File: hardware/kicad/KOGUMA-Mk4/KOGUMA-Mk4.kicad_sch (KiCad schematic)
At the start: 0 parts

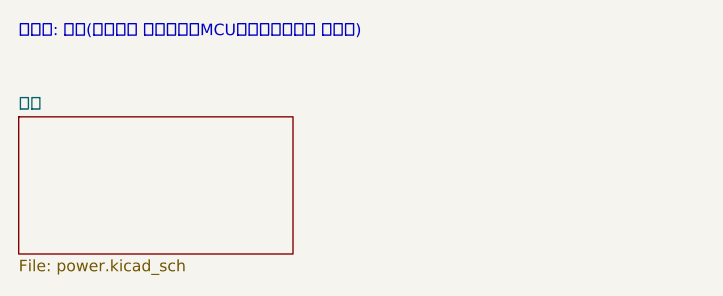
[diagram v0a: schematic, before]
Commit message: モーターのブロックの回路図を作り、MP6551 の電流計測(CM)で進めることを決める
- MP6551 の CM を調べた(精度は typ. のみ、+と−で約25%違う、応答の速さは書かれていない)。
  今の駆動方法(片側の下側のFETをずっと ON)なら電流が常に見えるので、専用ICなしで始め、
  1個ずつ・向きごとに校正する
- RREF を 6.2kΩ × 2 から 4.7kΩ × 2 に(+側が約4.3Aで振り切れるため)、CM に 1nF
- motor.kicad_sch: MP6551 × 2(VIN のパスコン、CM、SR、nFAULT、EN)と吸引ファン
- 記号 MP6551GQB・IRLML6344、フットプリント MPS_QFN-14_2.5x3mm を追加

Co-Authored-By: Claude Opus 5.5 <noreply@anthropic.com>
Claude-Session: https://claude.ai/code/session_01H2Zvpqxqu2v63zaiCMmfT3
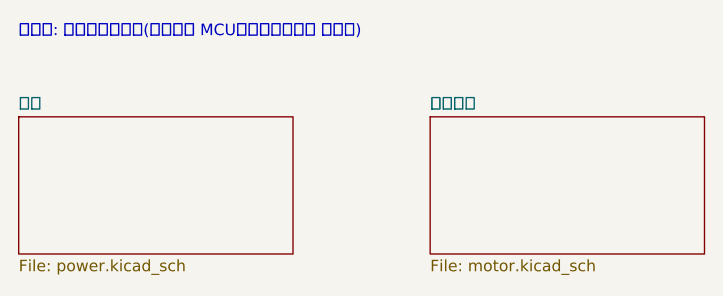
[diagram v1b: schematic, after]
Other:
- added sheet モーター (motor.kicad_sch)
- note added: "シート: 電源・モーター(これから MCU・センサ・表示 を足す)"
- note removed: "シート: 電源(これから モーター・MCU・センサ・表示 を足す)"
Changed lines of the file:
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@@
 		(rev "0.1")
 	)
-	(text "シート: 電源(これから モーター・MCU・センサ・表示 を足す)"
+	(text "シート: 電源・モーター(これから MCU・センサ・表示 を足す)"
 		(exclude_from_sim no)
 		(at 25.4 20.32 0)
@@
 		(instances
 			(project "KOGUMA-Mk4"
-				(path "/9b7d9cce-e694-4ccb-908f-cf46129b4ffc"
+				(path "/b4ecac63-bf9d-5a4c-873b-2154e676a044"
 					(page "2")
 				)
 			)
+		)
+	)
+	(sheet
+		(at 71.12 30.48)
+		(size 30.48 15.24)
+		(exclude_from_sim no)
+		(in_bom yes)
+		(on_board yes)
+		(dnp no)
+		(fields_autoplaced yes)
+		(stroke
+			(width 0.1524)
+			(type solid)
+		)
+		(fill
+			(color 0 0 0 0.0000)
+		)
+		(property "Sheetname" "モーター"
+			(at 71.12 29.7684 0)
+			(effects
+				(font
+					(size 1.27 1.27)
+				)
+				(justify left bottom)
+			)
+		)
+		(property "Sheetfile" "motor.kicad_sch"
+			(at 71.12 46.3046 0)
+			(effects
+				(font
+					(size 1.27 1.27)
+				)
+				(justify left top)
+			)
+		)
+		(instances
+			(project "KOGUMA-Mk4"
+				(path "/b4ecac63-bf9d-5a4c-873b-2154e676a044"
+					(page "3")
+				)
+			)

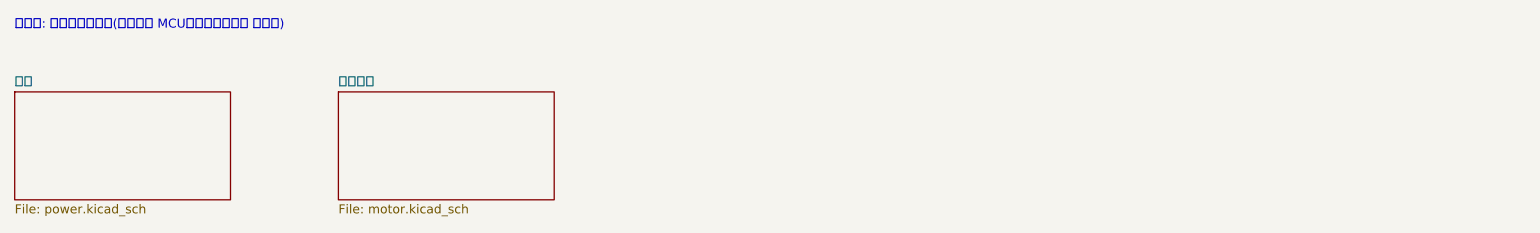
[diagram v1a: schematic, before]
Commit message: MCU のシートを作る(STM32H725RGVx、Direct SMPS、パスコン)
- mcu.kicad_sch: pinmap.md の41本をグローバルラベルで出す(ネットリストで一致を確認)、
  SMPS は DS13311 の図17「Direct SMPS supply」のとおり(L1 2.2µH、VFBSMPS 10µF、VLXSMPS 220pF)、
  VDD ごとの 100nF + 4.7µF、VBAT 100nF、VDDA はフェライトビーズ + 1µF + 100nF、BOOT0 10kΩ、NRST 100nF
- VCAP を 2.2µF × 2 から 100nF × 2 に(表15の注1: LDO を使わないとき。VFQFPN68 は Direct SMPS 専用)
- STM32H725RGVx の記号をプロジェクトに写し、ピンの種類を直す(VLXSMPS を出力、重ねた VCAP を passive)

Co-Authored-By: Claude Opus 5.5 <noreply@anthropic.com>
Claude-Session: https://claude.ai/code/session_01H2Zvpqxqu2v63zaiCMmfT3
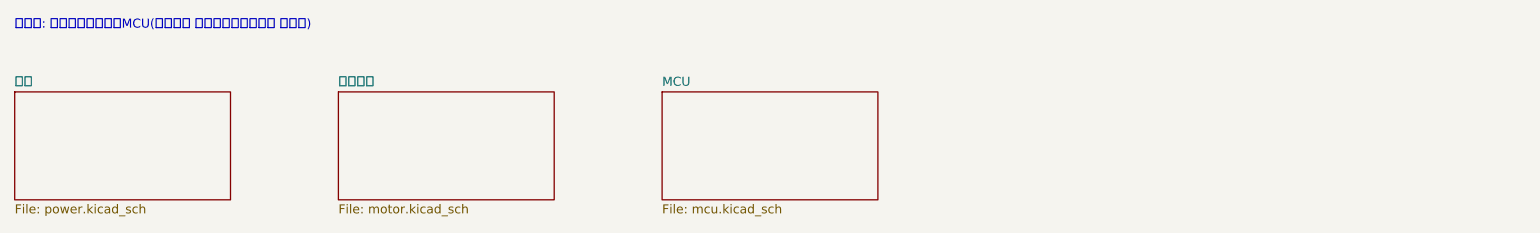
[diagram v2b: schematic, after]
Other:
- added sheet MCU (mcu.kicad_sch)
- note added: "シート: 電源・モーター・MCU(これから センサ・表示・通信 を足す)"
- note removed: "シート: 電源・モーター(これから MCU・センサ・表示 を足す)"
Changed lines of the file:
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@@
 		(rev "0.1")
 	)
-	(text "シート: 電源・モーター(これから MCU・センサ・表示 を足す)"
+	(text "シート: 電源・モーター・MCU(これから センサ・表示・通信 を足す)"
 		(exclude_from_sim no)
 		(at 25.4 20.32 0)
@@
 				)
 			)
+		)
+	)
+	(sheet
+		(at 116.84 30.48)
+		(size 30.48 15.24)
+		(exclude_from_sim no)
+		(in_bom yes)
+		(on_board yes)
+		(dnp no)
+		(fields_autoplaced yes)
+		(stroke
+			(width 0.1524)
+			(type solid)
+		)
+		(fill
+			(color 0 0 0 0.0000)
+		)
+		(property "Sheetname" "MCU"
+			(at 116.84 29.7684 0)
+			(effects
+				(font
+					(size 1.27 1.27)
+				)
+				(justify left bottom)
+			)
+		)
+		(property "Sheetfile" "mcu.kicad_sch"
+			(at 116.84 46.3046 0)
+			(effects
+				(font
+					(size 1.27 1.27)
+				)
+				(justify left top)
+			)
+		)
+		(instances
+			(project "KOGUMA-Mk4"
+				(path "/b4ecac63-bf9d-5a4c-873b-2154e676a044"
+					(page "4")
+				)
+			)

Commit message: センサのシートを作る(壁センサ 4ch、IMU、エンコーダの基板への線)
- sensor.kicad_sch(A3): MK3 の回路(docs/reference)を 3.3V・1個ずつ駆動に合わせて描く。
  発光 OPV332 + NJU6080(20Ω、10mA)× 4、受光 SFH 229 FA + AD8606(820k ∥ 2.2p、PD_BIAS 0.148V)× 4、
  IMU LSM6DSR(SPI3)、エンコーダの基板への6本の線 × 2
- 発光は MK3 と同じく対角の2個ずつ(MK3 のソフトの WallLED_12 / WallLED_34)。
  ネット名を WALL_LED_L / WALL_LED_R から WALL_LED_FL_R / WALL_LED_L_FR に変える
- 記号 NJU6080・LSM6DSR を追加。生成に使う記号の継承(extends)と複数ユニットに対応

Co-Authored-By: Claude Opus 5.5 <noreply@anthropic.com>
Claude-Session: https://claude.ai/code/session_01H2Zvpqxqu2v63zaiCMmfT3
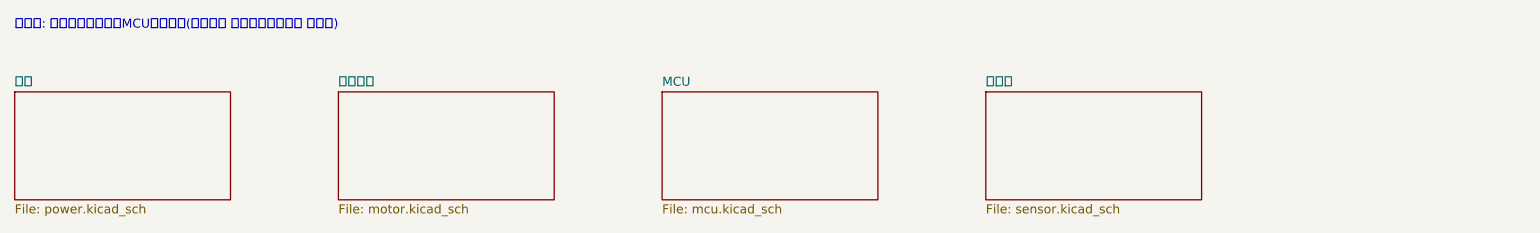
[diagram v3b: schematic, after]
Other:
- added sheet センサ (sensor.kicad_sch)
- note added: "シート: 電源・モーター・MCU・センサ(これから 表示・入力・通信 を足す)"
- note removed: "シート: 電源・モーター・MCU(これから センサ・表示・通信 を足す)"
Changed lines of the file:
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@@
 		(rev "0.1")
 	)
-	(text "シート: 電源・モーター・MCU(これから センサ・表示・通信 を足す)"
+	(text "シート: 電源・モーター・MCU・センサ(これから 表示・入力・通信 を足す)"
 		(exclude_from_sim no)
 		(at 25.4 20.32 0)
@@
 				)
 			)
+		)
+	)
+	(sheet
+		(at 162.56 30.48)
+		(size 30.48 15.24)
+		(exclude_from_sim no)
+		(in_bom yes)
+		(on_board yes)
+		(dnp no)
+		(fields_autoplaced yes)
+		(stroke
+			(width 0.1524)
+			(type solid)
+		)
+		(fill
+			(color 0 0 0 0.0000)
+		)
+		(property "Sheetname" "センサ"
+			(at 162.56 29.7684 0)
+			(effects
+				(font
+					(size 1.27 1.27)
+				)
+				(justify left bottom)
+			)
+		)
+		(property "Sheetfile" "sensor.kicad_sch"
+			(at 162.56 46.3046 0)
+			(effects
+				(font
+					(size 1.27 1.27)
+				)
+				(justify left top)
+			)
+		)
+		(instances
+			(project "KOGUMA-Mk4"
+				(path "/b4ecac63-bf9d-5a4c-873b-2154e676a044"
+					(page "5")
+				)
+			)

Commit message: 表示・入力・通信のシートを作る(LED 7個、ブザー、スイッチ、デバッグの端子)
- ui.kicad_sch: LED(GPIO H で点灯、1kΩ)、ブザー(2N7002、還流ダイオード)、
  スイッチ(10kΩ プルアップ + 100nF)、デバッグの端子 J7(ToraNeko.Mk3 の J6 と同じ並び、
  STLINK-V3MODS)、UART_RX のテストパッド
- これで全シートがそろい、ERC のエラーとラベルの相手がいない警告がなくなった

Co-Authored-By: Claude Opus 5.5 <noreply@anthropic.com>
Claude-Session: https://claude.ai/code/session_01H2Zvpqxqu2v63zaiCMmfT3
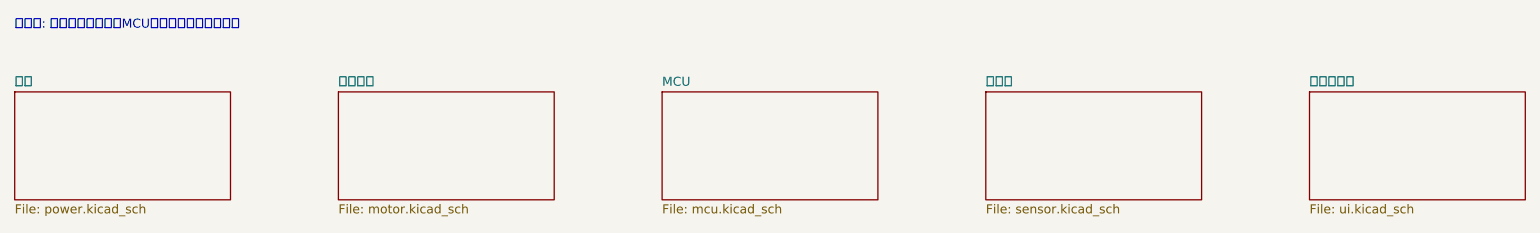
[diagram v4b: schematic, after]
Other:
- added sheet 表示・通信 (ui.kicad_sch)
- note added: "シート: 電源・モーター・MCU・センサ・表示と通信"
- note removed: "シート: 電源・モーター・MCU・センサ(これから 表示・入力・通信 を足す)"
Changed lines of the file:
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@@
 		(rev "0.1")
 	)
-	(text "シート: 電源・モーター・MCU・センサ(これから 表示・入力・通信 を足す)"
+	(text "シート: 電源・モーター・MCU・センサ・表示と通信"
 		(exclude_from_sim no)
 		(at 25.4 20.32 0)
@@
 				)
 			)
+		)
+	)
+	(sheet
+		(at 208.28 30.48)
+		(size 30.48 15.24)
+		(exclude_from_sim no)
+		(in_bom yes)
+		(on_board yes)
+		(dnp no)
+		(fields_autoplaced yes)
+		(stroke
+			(width 0.1524)
+			(type solid)
+		)
+		(fill
+			(color 0 0 0 0.0000)
+		)
+		(property "Sheetname" "表示・通信"
+			(at 208.28 29.7684 0)
+			(effects
+				(font
+					(size 1.27 1.27)
+				)
+				(justify left bottom)
+			)
+		)
+		(property "Sheetfile" "ui.kicad_sch"
+			(at 208.28 46.3046 0)
+			(effects
+				(font
+					(size 1.27 1.27)
+				)
+				(justify left top)
+			)
+		)
+		(instances
+			(project "KOGUMA-Mk4"
+				(path "/b4ecac63-bf9d-5a4c-873b-2154e676a044"
+					(page "6")
+				)
+			)
